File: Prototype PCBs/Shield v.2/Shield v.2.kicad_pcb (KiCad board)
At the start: 2 copper layers, 99.7 x 125.1 mm, 85 parts, among them J1 JumpSwitch, J2 JumpSwitch, J3 JumpSwitch, J4 JumpSwitch, J5 JumpSwitch, J6 JumpSwitch, J7 JumpSwitch, J8 JumpSwitch, SW1 SW_Push, SW10 SW_Push, SW2 SW_Push, SW3 SW_Push, SW4 SW_Push, SW5 SW_Push, SW6 SW_Push, SW7 SW_Push, SW8 SW_Push, SW9 SW_Push, U1 MCP23017_SS

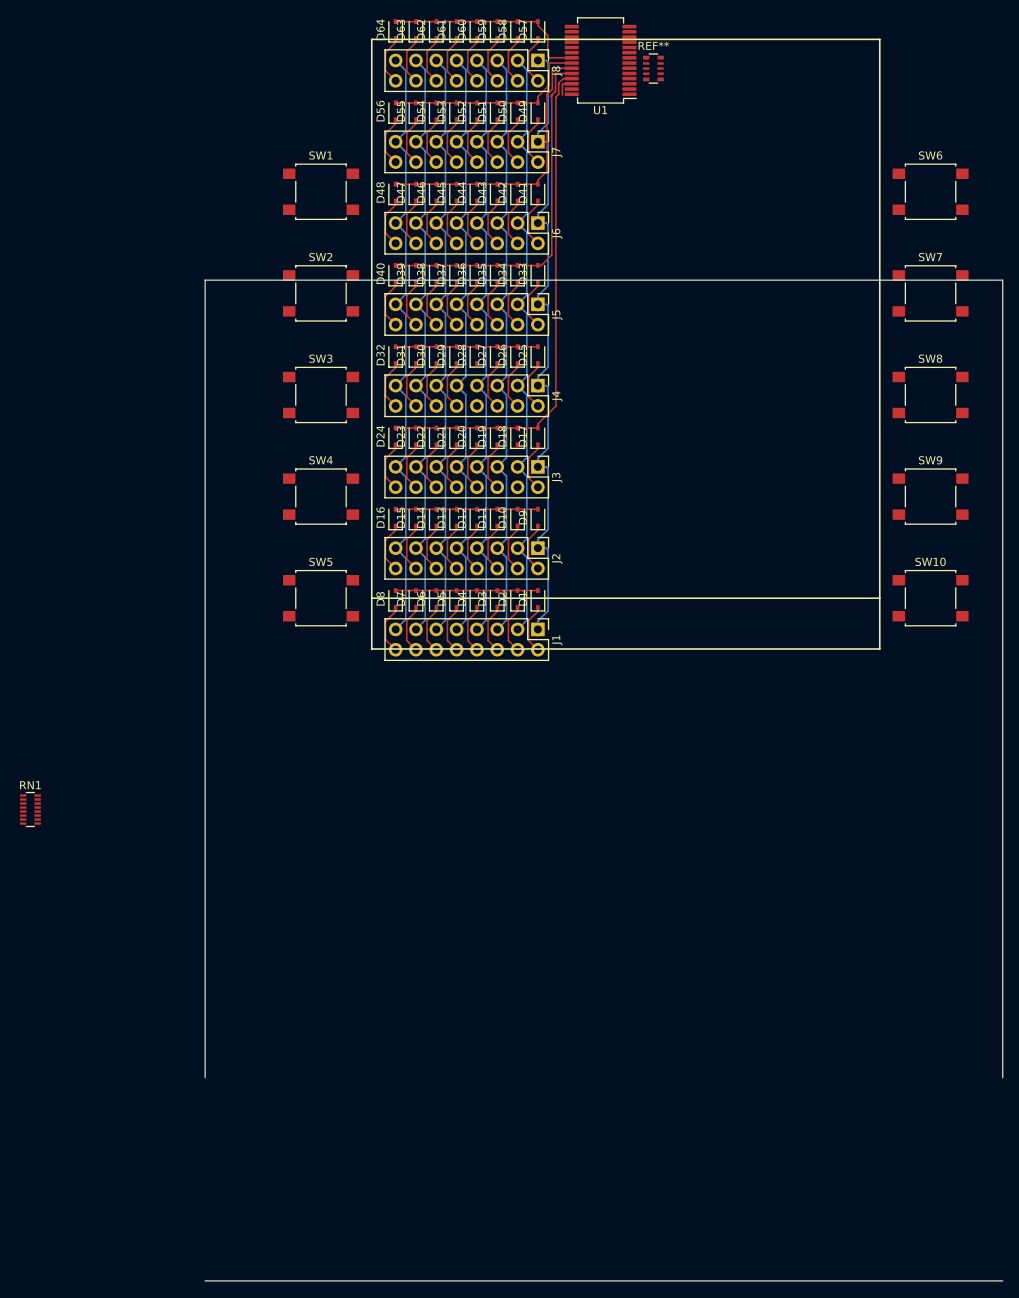
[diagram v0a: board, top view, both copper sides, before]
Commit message: V2 Panels. Matrix Input Test Sketch
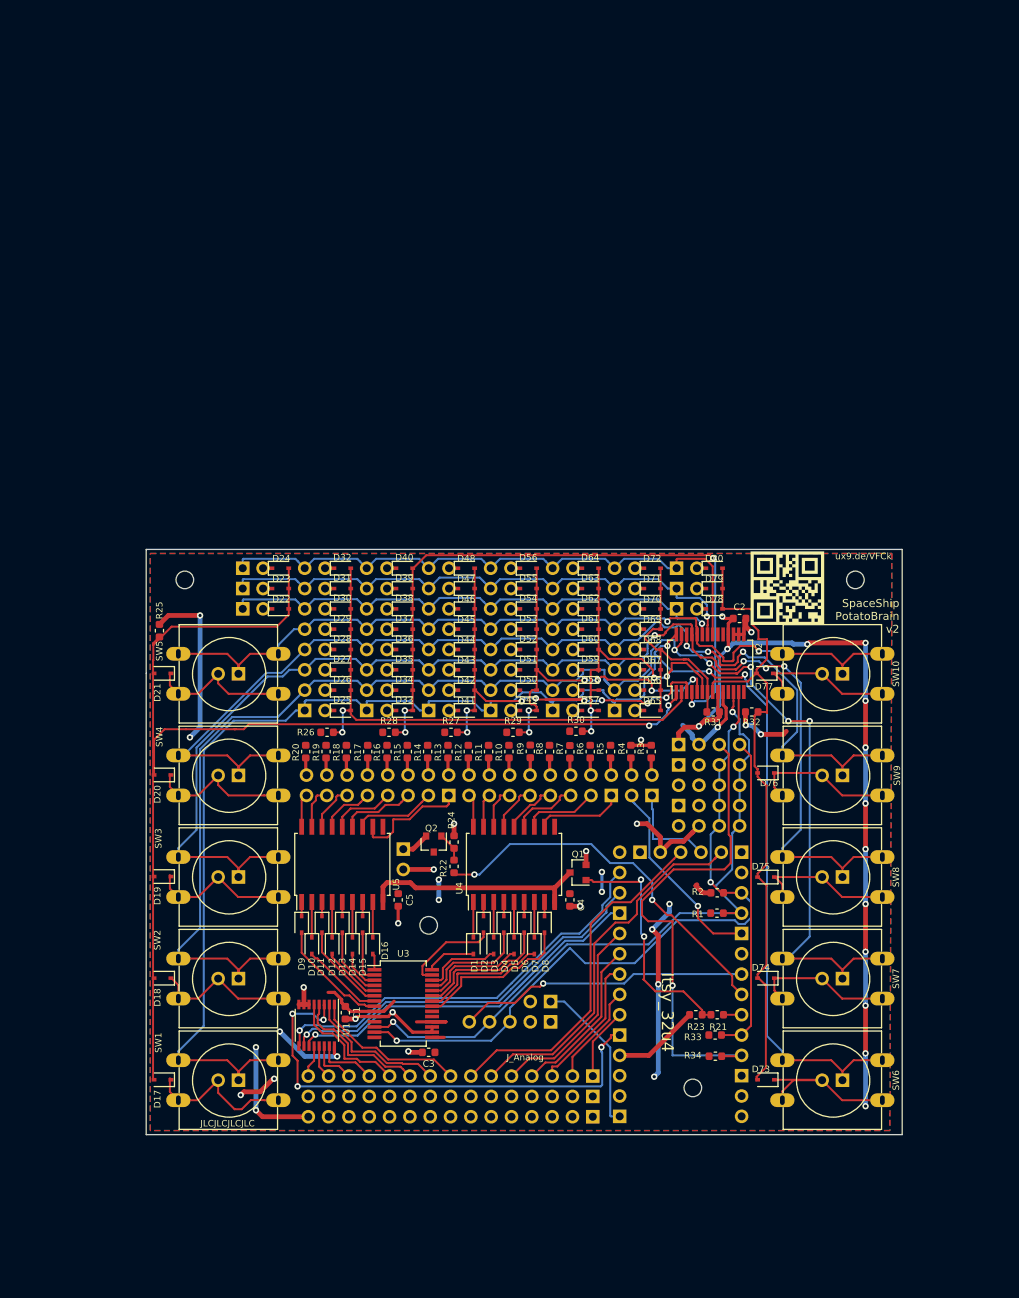
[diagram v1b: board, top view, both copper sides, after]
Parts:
- removed REF**: R_Array_Convex_5x0603, Resistor_SMD:R_Array_Convex_5x0603
- removed RN1: R_Network08_US, Resistor_SMD:R_Array_Convex_8x0602
- added A: Conn_01x15, Connector_PinHeader_2.54mm:PinHeader_1x15_P2.54mm_Vertical, B.Cu at (157.7, 123.0)
- added C1: C, Capacitor_SMD:C_0603_1608Metric, F.Cu at (126.7, 115.1)
- added C2: C, Capacitor_SMD:C_0603_1608Metric, F.Cu at (176.0, 65.8)
- added C3: C, Capacitor_SMD:C_0603_1608Metric, F.Cu at (137.2, 120.0)
- added C4: C, Capacitor_SMD:C_0603_1608Metric, F.Cu at (154.8, 101.0)
- added C5: C, Capacitor_SMD:C_0603_1608Metric, F.Cu at (133.3, 101.0)
- added D65: 1N4148, Diode_SMD:D_SOD-323, F.Cu at (165.1, 77.3)
- added D66: 1N4148, Diode_SMD:D_SOD-323, F.Cu at (165.1, 74.7)
- added D67: 1N4148, Diode_SMD:D_SOD-323, F.Cu at (165.1, 72.2)
- added D68: 1N4148, Diode_SMD:D_SOD-323, F.Cu at (165.1, 69.7)
- added D69: 1N4148, Diode_SMD:D_SOD-323, F.Cu at (165.1, 67.1)
- added D70: 1N4148, Diode_SMD:D_SOD-323, F.Cu at (165.1, 64.6)
- added D71: 1N4148, Diode_SMD:D_SOD-323, F.Cu at (165.1, 62.0)
- added D72: 1N4148, Diode_SMD:D_SOD-323, F.Cu at (165.1, 59.5)
- added D73: 1N4148, Diode_SMD:D_SOD-323, F.Cu at (179.3, 123.4)
- added D74: 1N4148, Diode_SMD:D_SOD-323, F.Cu at (179.3, 110.7)
- added D75: 1N4148, Diode_SMD:D_SOD-323, F.Cu at (179.3, 98.1)
- added D76: 1N4148, Diode_SMD:D_SOD-323, F.Cu at (179.3, 85.1)
- added D77: 1N4148, Diode_SMD:D_SOD-323, F.Cu at (179.2, 72.6)
- added D78: 1N4148, Diode_SMD:D_SOD-323, F.Cu at (172.8, 64.6)
- added D79: 1N4148, Diode_SMD:D_SOD-323, F.Cu at (172.8, 62.0)
- added D80: 1N4148, Diode_SMD:D_SOD-323, F.Cu at (172.8, 59.5)
- added G: Conn_01x15, Connector_PinHeader_2.54mm:PinHeader_1x15_P2.54mm_Vertical, B.Cu at (157.7, 125.5)
- added J10: i2cA, Connector_PinHeader_2.54mm:PinHeader_2x04_P2.54mm_Vertical, B.Cu at (168.4, 84.1)
- added J11: i2cB, Connector_PinHeader_2.54mm:PinHeader_2x04_P2.54mm_Vertical, B.Cu at (168.4, 89.2)
- added J14: Conn_SysBut, Connector_PinHeader_2.54mm:PinHeader_1x04_P2.54mm_Vertical, B.Cu at (168.4, 81.5)
- added J15: Conn_bLight, Connector_PinHeader_2.54mm:PinHeader_1x02_P2.54mm_Vertical, B.Cu at (134.0, 94.6)
- added J16: Conn_SysLED, Connector_PinHeader_2.54mm:PinHeader_2x02_P2.54mm_Vertical, B.Cu at (165.1, 87.9)
- added J17: LEDs_A, Connector_PinHeader_2.54mm:PinHeader_2x08_P2.54mm_Vertical, B.Cu at (160.0, 87.9)
- added J18: LEDs_B, Connector_PinHeader_2.54mm:PinHeader_2x08_P2.54mm_Vertical, B.Cu at (139.7, 87.9)
- added J19F2: Jumper_NO_Small, Connector_PinHeader_2.54mm:PinHeader_1x02_P2.54mm_Vertical, B.Cu at (113.9, 64.6)
- added J19G1: Jumper_NO_Small, Connector_PinHeader_2.54mm:PinHeader_1x02_P2.54mm_Vertical, B.Cu at (113.9, 62.0)
- added J26F1: Jumper_NO_Small, Connector_PinHeader_2.54mm:PinHeader_1x02_P2.54mm_Vertical, B.Cu at (168.1, 64.6)
- added J26G1: Jumper_NO_Small, Connector_PinHeader_2.54mm:PinHeader_1x02_P2.54mm_Vertical, B.Cu at (168.1, 62.0)
- added J9: Conn_Reset, Connector_PinHeader_2.54mm:PinHeader_1x02_P2.54mm_Vertical, B.Cu at (152.4, 113.7)
- added J_c0: Jumper_NO_Small, Connector_PinHeader_2.54mm:PinHeader_1x02_P2.54mm_Vertical, B.Cu at (113.9, 59.5)
- added J_c0_r0: Jumper_NO_Small, Connector_PinHeader_2.54mm:PinHeader_1x02_P2.54mm_Vertical, B.Cu at (113.4, 123.5)
- added J_c0_r1: Jumper_NO_Small, Connector_PinHeader_2.54mm:PinHeader_1x02_P2.54mm_Vertical, B.Cu at (113.4, 110.8)
- added J_c0_r2: Jumper_NO_Small, Connector_PinHeader_2.54mm:PinHeader_1x02_P2.54mm_Vertical, B.Cu at (113.4, 98.1)
- added J_c0_r3: Jumper_NO_Small, Connector_PinHeader_2.54mm:PinHeader_1x02_P2.54mm_Vertical, B.Cu at (113.4, 85.4)
- added J_c0_r4: Jumper_NO_Small, Connector_PinHeader_2.54mm:PinHeader_1x02_P2.54mm_Vertical, B.Cu at (113.4, 72.7)
- added J_c1: JumpSwitch, Connector_PinHeader_2.54mm:PinHeader_2x08_P2.54mm_Vertical, B.Cu at (121.7, 77.3)
- added J_c2: JumpSwitch, Connector_PinHeader_2.54mm:PinHeader_2x08_P2.54mm_Vertical, B.Cu at (129.4, 77.3)
- added J_c3: JumpSwitch, Connector_PinHeader_2.54mm:PinHeader_2x08_P2.54mm_Vertical, B.Cu at (137.2, 77.3)
- added J_c4: JumpSwitch, Connector_PinHeader_2.54mm:PinHeader_2x08_P2.54mm_Vertical, B.Cu at (144.9, 77.3)
- added J_c5: JumpSwitch, Connector_PinHeader_2.54mm:PinHeader_2x08_P2.54mm_Vertical, B.Cu at (152.7, 77.3)
- added J_c6: JumpSwitch, Connector_PinHeader_2.54mm:PinHeader_2x08_P2.54mm_Vertical, B.Cu at (160.4, 77.3)
- added J_c7: Jumper_NO_Small, Connector_PinHeader_2.54mm:PinHeader_1x02_P2.54mm_Vertical, B.Cu at (168.1, 59.5)
- added J_c7_r0: Jumper_NO_Small, Connector_PinHeader_2.54mm:PinHeader_1x02_P2.54mm_Vertical, B.Cu at (188.9, 123.5)
- added J_c7_r1: Jumper_NO_Small, Connector_PinHeader_2.54mm:PinHeader_1x02_P2.54mm_Vertical, B.Cu at (188.9, 110.8)
- added J_c7_r2: Jumper_NO_Small, Connector_PinHeader_2.54mm:PinHeader_1x02_P2.54mm_Vertical, B.Cu at (188.9, 98.1)
- added J_c7_r3: Jumper_NO_Small, Connector_PinHeader_2.54mm:PinHeader_1x02_P2.54mm_Vertical, B.Cu at (188.9, 85.4)
- added J_c7_r4: Jumper_NO_Small, Connector_PinHeader_2.54mm:PinHeader_1x02_P2.54mm_Vertical, B.Cu at (188.9, 72.7)
- added Mount1: MountingHole_2.2mm_M2, MountingHole:MountingHole_2.2mm_M2, F.Cu at (106.7, 61.0)
- added Mount2: MountingHole_2.2mm_M2, MountingHole:MountingHole_2.2mm_M2, F.Cu at (190.5, 61.0)
- added Mount3: MountingHole_2.2mm_M2, MountingHole:MountingHole_2.2mm_M2, F.Cu at (170.2, 124.5)
- added Mount4: MountingHole_2.2mm_M2, MountingHole:MountingHole_2.2mm_M2, F.Cu at (137.2, 104.1)
- added Q1: Q_NMOS_DIM, Package_TO_SOT_SMD:SOT-23, F.Cu at (155.8, 97.5)
- added Q2: Q_NMOS_DIM, Package_TO_SOT_SMD:SOT-23, F.Cu at (137.8, 94.0)
- added QR*****: ux9.de/VFCk, ux9.de_VFCk, B.Cu at (182.5, 64.0)
- added QR*****: ux9.de/VFCk, ux9.de_VFCk, F.Cu at (182.0, 62.0)
- added R1: R4.7k, Resistor_SMD:R_0603_1608Metric, F.Cu at (173.2, 102.6)
- added R10: R, Resistor_SMD:R_0603_1608Metric, F.Cu at (147.2, 82.4)
- added R11: R, Resistor_SMD:R_0603_1608Metric, F.Cu at (144.7, 82.4)
- added R12: R, Resistor_SMD:R_0603_1608Metric, F.Cu at (142.1, 82.4)
- added R13: R, Resistor_SMD:R_0603_1608Metric, F.Cu at (139.6, 82.4)
- added R14: R, Resistor_SMD:R_0603_1608Metric, F.Cu at (137.0, 82.4)
- added R15: R, Resistor_SMD:R_0603_1608Metric, F.Cu at (134.5, 82.4)
- added R16: R, Resistor_SMD:R_0603_1608Metric, F.Cu at (132.0, 82.4)
- added R17: R, Resistor_SMD:R_0603_1608Metric, F.Cu at (129.5, 82.4)
- added R18: R, Resistor_SMD:R_0603_1608Metric, F.Cu at (126.9, 82.4)
- added R19: R, Resistor_SMD:R_0603_1608Metric, F.Cu at (124.3, 82.4)
- added R2: R4.7k, Resistor_SMD:R_0603_1608Metric, F.Cu at (173.2, 100.1)
- added R20: R, Resistor_SMD:R_0603_1608Metric, F.Cu at (121.8, 82.4)
- added R21: R1k, Resistor_SMD:R_0603_1608Metric, F.Cu at (173.2, 115.3)
- added R22: R1k, Resistor_SMD:R_0603_1608Metric, F.Cu at (140.3, 96.8)
- added R23: R4.7k, Resistor_SMD:R_0603_1608Metric, F.Cu at (170.6, 115.3)
- added R24: R4.7k, Resistor_SMD:R_0603_1608Metric, F.Cu at (140.3, 93.7)
- added R25: R4.7k, Resistor_SMD:R_0603_1608Metric, F.Cu at (103.5, 67.3)
- added R26: R4.7k, Resistor_SMD:R_0603_1608Metric, F.Cu at (124.5, 80.0)
- added R27: R4.7k, Resistor_SMD:R_0603_1608Metric, F.Cu at (140.0, 80.0)
- added R28: R4.7k, Resistor_SMD:R_0603_1608Metric, F.Cu at (132.2, 80.0)
- added R29: R4.7k, Resistor_SMD:R_0603_1608Metric, F.Cu at (147.7, 80.0)
- added R3: R, Resistor_SMD:R_0603_1608Metric, F.Cu at (165.0, 82.4)
- added R30: R4.7k, Resistor_SMD:R_0603_1608Metric, F.Cu at (155.6, 79.9)
- added R31: R4.7k, Resistor_SMD:R_0603_1608Metric, F.Cu at (172.7, 77.5)
- added R32: R4.7k, Resistor_SMD:R_0603_1608Metric, F.Cu at (177.5, 77.5)
- added R33: R4.7k, Resistor_SMD:R_0603_1608Metric, F.Cu at (173.0, 117.9)
- added R34: R4.7k, Resistor_SMD:R_0603_1608Metric, F.Cu at (173.0, 120.5)
- added R4: R, Resistor_SMD:R_0603_1608Metric, F.Cu at (162.4, 82.4)
- added R5: R, Resistor_SMD:R_0603_1608Metric, F.Cu at (159.9, 82.4)
- added R6: R, Resistor_SMD:R_0603_1608Metric, F.Cu at (157.4, 82.4)
- added R7: R, Resistor_SMD:R_0603_1608Metric, F.Cu at (154.8, 82.4)
- added R8: R, Resistor_SMD:R_0603_1608Metric, F.Cu at (152.3, 82.4)
- added R9: R, Resistor_SMD:R_0603_1608Metric, F.Cu at (149.9, 82.4)
- added U2: MCP23017_0x20_in, Package_SO:SSOP-28_5.3x10.2mm_P0.65mm, F.Cu at (172.3, 71.4)
- added U3: MCP23017_0x21_out, Package_SO:SSOP-28_5.3x10.2mm_P0.65mm, F.Cu at (134.0, 113.9)
- added U4: ULN2803A, Package_SO:SOIC-18W_7.5x11.6mm_P1.27mm, F.Cu at (147.8, 96.5)
- added U5: ULN2803A, Package_SO:SOIC-18W_7.5x11.6mm_P1.27mm, F.Cu at (126.4, 96.5)
- added V: Conn_01x15, Connector_PinHeader_2.54mm:PinHeader_1x15_P2.54mm_Vertical, B.Cu at (157.7, 128.1)
- D1, D10, D11, D12, D13, D14, D15, D16, D2, D3, D4, D5, D6, D7, D8, D9: value 1N4148 -> D
- J1, J3, J8: value JumpSwitch -> Conn_01x04; footprint Connector_PinHeader_2.54mm:PinHeader_2x08_P2.54mm_Vertical -> Connector_PinHeader_2.54mm:PinHeader_1x04_P2.54mm_Vertical; moved to B.Cu
- J2: value JumpSwitch -> Conn_01x06; footprint Connector_PinHeader_2.54mm:PinHeader_2x08_P2.54mm_Vertical -> Connector_PinHeader_2.54mm:PinHeader_1x06_P2.54mm_Vertical; moved to B.Cu
- J4: value JumpSwitch -> Conn_01x05; footprint Connector_PinHeader_2.54mm:PinHeader_2x08_P2.54mm_Vertical -> Connector_PinHeader_2.54mm:PinHeader_1x05_P2.54mm_Vertical; moved to B.Cu
- J5: value JumpSwitch -> Motor; footprint Connector_PinHeader_2.54mm:PinHeader_2x08_P2.54mm_Vertical -> Connector_PinHeader_2.54mm:PinHeader_1x05_P2.54mm_Vertical; moved to B.Cu
- J6: value JumpSwitch -> Conn_01x03; footprint Connector_PinHeader_2.54mm:PinHeader_2x08_P2.54mm_Vertical -> Connector_PinHeader_2.54mm:PinHeader_1x03_P2.54mm_Vertical; moved to B.Cu
- J7: value JumpSwitch -> Conn_01x07; footprint Connector_PinHeader_2.54mm:PinHeader_2x08_P2.54mm_Vertical -> Connector_PinHeader_2.54mm:PinHeader_1x07_P2.54mm_Vertical; moved to B.Cu
- SW1, SW10, SW2, SW3, SW4, SW5, SW6, SW7, SW8, SW9: footprint Button_Switch_SMD:SW_SPST_B3S-1000 -> Kicad Parts:SW_PUSH-12mm_widepinholes
- U1: value MCP23017_SS -> 74HC4051; footprint Package_SO:SSOP-28_5.3x10.2mm_P0.65mm -> Package_SO:SSOP-16_3.9x4.9mm_P0.635mm
- moved U1 125.7 mm to (123.2, 116.6), turned to 270 degrees
- moved SW6 110.1 mm to (181.4, 121.0)
- moved SW1 110.0 mm to (105.9, 121.0)
- moved J6 109.6 mm to (176.3, 122.9), turned to 180 degrees
- moved J7 102.2 mm to (176.3, 105.2), turned to 180 degrees
- moved J8 102.2 mm to (176.3, 95.0), turned to 180 degrees
- moved D17 93.1 mm to (103.9, 123.4), turned to 180 degrees
- moved J5 89.7 mm to (152.4, 116.2), turned to 90 degrees
- moved D57 85.3 mm to (157.4, 77.3), turned to 0 degrees
- moved SW7 85.2 mm to (181.4, 108.3)
- moved SW2 85.0 mm to (105.9, 108.3)
- moved D58 83.0 mm to (157.4, 74.7), turned to 0 degrees
- moved D18 81.0 mm to (103.9, 110.7), turned to 180 degrees
- moved D59 80.8 mm to (157.4, 72.2), turned to 0 degrees
- moved D60 78.7 mm to (157.4, 69.7), turned to 0 degrees
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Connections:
- D1 pad 1: Net-(D1-Pad1) -> /O.B0
- D1 pad 2: /Input Matrix/input_c0 -> Net-(D1-Pad2)
- D10 pad 1: Net-(D10-Pad1) -> /O.A1
- D10 pad 2: /Input Matrix/input_c1 -> Net-(D10-Pad2)
- D11 pad 1: Net-(D11-Pad1) -> /O.A2
- D11 pad 2: /Input Matrix/input_c1 -> Net-(D11-Pad2)
- D12 pad 1: Net-(D12-Pad1) -> /O.A3
- D12 pad 2: /Input Matrix/input_c1 -> Net-(D12-Pad2)
- D13 pad 1: Net-(D13-Pad1) -> /O.A4
- D13 pad 2: /Input Matrix/input_c1 -> Net-(D13-Pad2)
- D14 pad 1: Net-(D14-Pad1) -> /O.A5
- D14 pad 2: /Input Matrix/input_c1 -> Net-(D14-Pad2)
- D15 pad 1: Net-(D15-Pad1) -> /O.A6
- D15 pad 2: /Input Matrix/input_c1 -> Net-(D15-Pad2)
- D16 pad 1: Net-(D16-Pad1) -> /O.A7
- D16 pad 2: /Input Matrix/input_c1 -> Net-(D16-Pad2)
- D17 pad 2: /Input Matrix/input_c2 -> /Input Matrix/input_c0
- D18 pad 2: /Input Matrix/input_c2 -> /Input Matrix/input_c0
- D19 pad 2: /Input Matrix/input_c2 -> /Input Matrix/input_c0
- D2 pad 1: Net-(D2-Pad1) -> /O.B1
- D2 pad 2: /Input Matrix/input_c0 -> Net-(D2-Pad2)
- D20 pad 2: /Input Matrix/input_c2 -> /Input Matrix/input_c0
- D21 pad 2: /Input Matrix/input_c2 -> /Input Matrix/input_c0
- D22 pad 2: /Input Matrix/input_c2 -> /Input Matrix/input_c0
- D23 pad 2: /Input Matrix/input_c2 -> /Input Matrix/input_c0
- D24 pad 2: /Input Matrix/input_c2 -> /Input Matrix/input_c0
- D25 pad 2: /Input Matrix/input_c3 -> /Input Matrix/input_c1
- D26 pad 2: /Input Matrix/input_c3 -> /Input Matrix/input_c1
- D27 pad 2: /Input Matrix/input_c3 -> /Input Matrix/input_c1
- D28 pad 2: /Input Matrix/input_c3 -> /Input Matrix/input_c1
- D29 pad 2: /Input Matrix/input_c3 -> /Input Matrix/input_c1
- D3 pad 1: Net-(D3-Pad1) -> /O.B2
- D30 pad 2: /Input Matrix/input_c3 -> /Input Matrix/input_c1
- D31 pad 2: /Input Matrix/input_c3 -> /Input Matrix/input_c1
- D32 pad 2: /Input Matrix/input_c3 -> /Input Matrix/input_c1
- D33 pad 2: /Input Matrix/input_c4 -> /Input Matrix/input_c2
- D34 pad 2: /Input Matrix/input_c4 -> /Input Matrix/input_c2
- D35 pad 2: /Input Matrix/input_c4 -> /Input Matrix/input_c2
- D36 pad 2: /Input Matrix/input_c4 -> /Input Matrix/input_c2
- D37 pad 2: /Input Matrix/input_c4 -> /Input Matrix/input_c2
- D38 pad 2: /Input Matrix/input_c4 -> /Input Matrix/input_c2
- D39 pad 2: /Input Matrix/input_c4 -> /Input Matrix/input_c2
- D4 pad 1: Net-(D4-Pad1) -> /O.B3
- D40 pad 2: /Input Matrix/input_c4 -> /Input Matrix/input_c2
- D41 pad 2: /Input Matrix/input_c5 -> /Input Matrix/input_c3
- D42 pad 2: /Input Matrix/input_c5 -> /Input Matrix/input_c3
- D43 pad 2: /Input Matrix/input_c5 -> /Input Matrix/input_c3
- D44 pad 2: /Input Matrix/input_c5 -> /Input Matrix/input_c3
- D45 pad 2: /Input Matrix/input_c5 -> /Input Matrix/input_c3
- D46 pad 2: /Input Matrix/input_c5 -> /Input Matrix/input_c3
- D47 pad 2: /Input Matrix/input_c5 -> /Input Matrix/input_c3
- D48 pad 2: /Input Matrix/input_c5 -> /Input Matrix/input_c3
- D49 pad 2: /Input Matrix/input_c6 -> /Input Matrix/input_c4
- D5 pad 1: Net-(D5-Pad1) -> /O.B4
- D50 pad 2: /Input Matrix/input_c6 -> /Input Matrix/input_c4
- D51 pad 2: /Input Matrix/input_c6 -> /Input Matrix/input_c4
- D52 pad 2: /Input Matrix/input_c6 -> /Input Matrix/input_c4
- D53 pad 2: /Input Matrix/input_c6 -> /Input Matrix/input_c4
- D54 pad 2: /Input Matrix/input_c6 -> /Input Matrix/input_c4
- D55 pad 2: /Input Matrix/input_c6 -> /Input Matrix/input_c4
- D56 pad 2: /Input Matrix/input_c6 -> /Input Matrix/input_c4
- D57 pad 2: /Input Matrix/input_c7 -> /Input Matrix/input_c5
- D58 pad 2: /Input Matrix/input_c7 -> /Input Matrix/input_c5
- D59 pad 2: /Input Matrix/input_c7 -> /Input Matrix/input_c5
- D6 pad 1: Net-(D6-Pad1) -> /O.B5
- D6 pad 2: /Input Matrix/input_c0 -> Net-(D6-Pad2)
- D60 pad 2: /Input Matrix/input_c7 -> /Input Matrix/input_c5
- D61 pad 2: /Input Matrix/input_c7 -> /Input Matrix/input_c5
- D62 pad 2: /Input Matrix/input_c7 -> /Input Matrix/input_c5
- D63 pad 2: /Input Matrix/input_c7 -> /Input Matrix/input_c5
- D64 pad 2: /Input Matrix/input_c7 -> /Input Matrix/input_c5
- D7 pad 1: Net-(D7-Pad1) -> /O.B6
- D7 pad 2: /Input Matrix/input_c0 -> Net-(D7-Pad2)
- D8 pad 1: Net-(D8-Pad1) -> /O.B7
- D8 pad 2: /Input Matrix/input_c0 -> Net-(D8-Pad2)
- D9 pad 1: Net-(D9-Pad1) -> /O.A0
- D9 pad 2: /Input Matrix/input_c1 -> Net-(D9-Pad2)
- J1 pad 1: /Input Matrix/input_r0 -> /RST
- J1 pad 2: Net-(D1-Pad1) -> +5V
- J1 pad 3: /Input Matrix/input_r1 -> /Aref
- J1 pad 4: Net-(D2-Pad1) -> GND
- J2 pad 1: /Input Matrix/input_r0 -> /A0
- J2 pad 2: Net-(D9-Pad1) -> /A1
- J2 pad 3: /Input Matrix/input_r1 -> /A2
- J2 pad 4: Net-(D10-Pad1) -> /A3
- J2 pad 5: /Input Matrix/input_r2 -> /A4
- J2 pad 6: Net-(D11-Pad1) -> /A5
- J3 pad 1: /Input Matrix/input_r0 -> /15
- J3 pad 2: Net-(D17-Pad1) -> /16
- J3 pad 3: /Input Matrix/input_r1 -> /14
- J3 pad 4: Net-(D18-Pad1) -> /3V
- J4 pad 1: /Input Matrix/input_r0 -> /En
- J4 pad 2: Net-(D25-Pad1) -> GND
- J4 pad 3: /Input Matrix/input_r1 -> /A8
- J4 pad 4: Net-(D26-Pad1) -> /A7
- J4 pad 5: /Input Matrix/input_r2 -> /A6
- J5 pad 1: /Input Matrix/input_r0 -> +5V
- J5 pad 2: Net-(D33-Pad1) -> GND
- J5 pad 3: /Input Matrix/input_r1 -> /SDA
- J5 pad 4: Net-(D34-Pad1) -> /SCL
- J5 pad 5: /Input Matrix/input_r2 -> /9*
- J6 pad 1: /Input Matrix/input_r0 -> /USB
- J6 pad 2: Net-(D41-Pad1) -> Net-(J6-Pad2)
- J6 pad 3: /Input Matrix/input_r1 -> /BAT
- J7 pad 1: /Input Matrix/input_r0 -> /5*
- J7 pad 2: Net-(D49-Pad1) -> /7
- J7 pad 3: /Input Matrix/input_r1 -> /9*
- J7 pad 4: Net-(D50-Pad1) -> /10*
- J7 pad 5: /Input Matrix/input_r2 -> /11*
- J7 pad 6: Net-(D51-Pad1) -> /12
- J7 pad 7: /Input Matrix/input_r3 -> /13
- J8 pad 1: /Input Matrix/input_r0 -> /RX
- J8 pad 2: Net-(D57-Pad1) -> /TX
- J8 pad 3: /Input Matrix/input_r1 -> /SDA
- J8 pad 4: Net-(D58-Pad1) -> /SCL
- SW1 pad 2: Net-(D1-Pad1) -> Net-(D17-Pad1)
- SW10 pad 2: Net-(D61-Pad1) -> Net-(D77-Pad1)
- SW2 pad 2: Net-(D2-Pad1) -> Net-(D18-Pad1)
- SW3 pad 2: Net-(D3-Pad1) -> Net-(D19-Pad1)
- SW4 pad 2: Net-(D4-Pad1) -> Net-(D20-Pad1)
- SW5 pad 2: Net-(D5-Pad1) -> Net-(D21-Pad1)
- SW6 pad 2: Net-(D57-Pad1) -> Net-(D73-Pad1)
- SW7 pad 2: Net-(D58-Pad1) -> Net-(D74-Pad1)
- SW8 pad 2: Net-(D59-Pad1) -> Net-(D75-Pad1)
- SW9 pad 2: Net-(D60-Pad1) -> Net-(D76-Pad1)
- U1 pad 1: /Input Matrix/input_r0 -> /uA4
- U1 pad 10: Net-(U1-Pad10) -> /16
- U1 pad 11: Net-(U1-Pad11) -> /15
- U1 pad 12: Net-(U1-Pad12) -> /uA3
- U1 pad 13: Net-(U1-Pad13) -> /uA0
- U1 pad 14: Net-(U1-Pad14) -> /uA1
- U1 pad 15: Net-(U1-Pad15) -> /uA2
- U1 pad 16: Net-(U1-Pad16) -> +5V
- U1 pad 2: /Input Matrix/input_r1 -> /uA6
- U1 pad 3: /Input Matrix/input_r3 -> /A0
- U1 pad 4: /Input Matrix/input_r2 -> /uA7
- U1 pad 5: /Input Matrix/input_r4 -> /uA5
- U1 pad 6: /Input Matrix/input_r5 -> GND
- U1 pad 7: /Input Matrix/input_r6 -> GND
- U1 pad 8: /Input Matrix/input_r7 -> GND
- U1 pad 9: Net-(U1-Pad9) -> /14
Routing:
- net +5V: track 0.00 -> 205.2 mm, vias 0 -> 30
- net /Input Matrix/input_c0: track 17.8 -> 153.9 mm, vias 0 -> 2
- net /Input Matrix/input_r0: track 89.5 -> 212.4 mm, vias 0 -> 3
- net /Input Matrix/input_r1: track 77.8 -> 191.3 mm, vias 0 -> 5
- net /SDA: track 0.00 -> 90.1 mm, vias 0 -> 3
- net /SCL: track 0.00 -> 87.5 mm, vias 0 -> 2
- net /Input Matrix/input_r2: track 77.8 -> 161.9 mm, vias 0 -> 4
- net GND: track 0.00 -> 76.4 mm, vias 0 -> 15
- net /13: track 0.00 -> 62.3 mm, vias 0 -> 1
- net /A0: track 0.00 -> 61.8 mm, vias 0 -> 4
- net /Input Matrix/input_r3: track 77.8 -> 137.1 mm, vias 0 -> 3
- net /Input Matrix/input_c7: track 25.7 -> 81.8 mm
- net /15: track 0.00 -> 52.4 mm, vias 0 -> 1
- net /14: track 0.00 -> 51.9 mm, vias 0 -> 1
- net /Input Matrix/input_c1: track 17.9 -> 66.9 mm, vias 0 -> 2
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- added copper zone on F.Cu, net +5V
- added copper zone on B.Cu, net GND
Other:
- board size 99.7 x 125.1 mm -> 94.5 x 73.2 mm
- net class Default: trace_width 0.2 -> 0.25
- net class Power added: clearance 0.2, trace_width 0.6, via_dia 0.8, via_drill 0.4
- board text added: "Analog"
- board text added: "G"
- board text added: "Itsy_32u4"
- board text added: "JLCJLCJLCJLC"
- board text added: "J_Analog"
- board text added: "LEDa"
- board text added: "LEDb"
- board text added: "MOT"
- board text added: "Motor"
- board text added: "NoteCard Area"
- board text added: "RST"
- board text added: "Reset"
- board text added: "S.B1"
- board text added: "S.B2"
- board text added: "SCL"
- board text added: "SDA"
- board text added: "SpaceShip PotatoBrain v2"
- board text added: "SysButton"
- board text added: "SysLED"
- board text added: "V"
- board text added: "backlight"
- board text added: "row0"
- board text added: "row1"
- board text added: "row2"
- board text added: "row3"
- board text added: "row4"
- board text added: "row5"
- board text added: "row6"
- board text added: "row7"

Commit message: Corrected Unavailable 74HC4051 footprint on Shield Board
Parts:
- U1: footprint Package_SO:SSOP-16_3.9x4.9mm_P0.635mm -> Package_SO:TSSOP-16_4.4x5mm_P0.65mm
- moved U1 0.46 mm to (123.2, 117.1)
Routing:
- net /uA4: track 19.3 -> 26.3 mm
- net /uA6: track 18.1 -> 24.1 mm
- net /uA5: track 15.6 -> 19.8 mm
- net /A0: track 61.8 -> 64.5 mm, vias 4 -> 2
- net /uA1: track 6.05 -> 3.57 mm
- net /15: track 52.4 -> 54.7 mm
- net /16: track 48.8 -> 51.0 mm
- net /uA7: track 17.5 -> 19.4 mm
- net /uA0: track 4.24 -> 5.35 mm
- net +5V: track 205.2 -> 204.2 mm
- net /14: track 51.9 -> 52.4 mm
- net /uA2: track 7.70 -> 7.13 mm
- net /uA3: track 4.05 -> 3.49 mm
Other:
- board text removed: "JLCJLCJLCJLC"
